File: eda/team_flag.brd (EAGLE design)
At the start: 40.6 x 40.6 mm, 20 parts, among them Q1 MOSFET-LOGIC-NCHANNELSMD, Q2 MOSFET-LOGIC-NCHANNELSMD, U1 ISL83491SOIC, U2 ATTINY1634

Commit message: Add some BOM metadata
* SMA-package diodes
* SOT23-3 MOSFETs
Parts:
- Q1, Q2: value MOSFET-LOGIC-NCHANNELSMD -> IRFML8244; device pie:SOT23-3-LOGIC -> pie:SOT23-3
- R3, R4: value 10K -> 10k
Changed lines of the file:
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@@
 <layer number="1" name="Top" color="4" fill="1" visible="yes" active="yes"/>
 <layer number="2" name="Route2" color="1" fill="3" visible="no" active="no"/>
-<layer number="3" name="Route3" color="4" fill="3" visible="no" active="no"/>
-<layer number="4" name="Route4" color="1" fill="4" visible="no" active="no"/>
+<layer number="3" name="Route3" color="20" fill="3" visible="no" active="no"/>
+<layer number="4" name="Route4" color="21" fill="4" visible="no" active="no"/>
 <layer number="5" name="Route5" color="4" fill="4" visible="no" active="no"/>
 <layer number="6" name="Route6" color="1" fill="8" visible="no" active="no"/>
@@
 <element name="U$2" library="pie" package="OSHW-LOGO-S" value="" x="16.764" y="31.75"/>
 <element name="U$1" library="pie" package="PIE-LOGO-SMALL" value="" x="2.921" y="17.272"/>
-<element name="Q1" library="pie" package="SOT23-3-LOGIC" value="MOSFET-LOGIC-NCHANNELSMD" x="19.304" y="13.208" smashed="yes">
+<element name="Q1" library="pie" package="SOT23-3" value="IRFML8244" x="19.304" y="13.208" smashed="yes">
 <attribute name="NAME" x="22.225" y="14.1097" size="0.635" layer="25" font="vector" rot="R180" align="top-left"/>
-<attribute name="PIE_DIGIKEY-PN" value="DMN65D8L-7DICT-ND" x="19.304" y="13.208" size="1.778" layer="27" display="off"/>
-</element>
-<element name="Q2" library="pie" package="SOT23-3-LOGIC" value="MOSFET-LOGIC-NCHANNELSMD" x="14.224" y="13.208" smashed="yes">
+<attribute name="PIE-INT-REF-NUM" value="NMOS" x="19.304" y="13.208" size="1.778" layer="27" display="off"/>
+</element>
+<element name="Q2" library="pie" package="SOT23-3" value="IRFML8244" x="14.224" y="13.208" smashed="yes">
 <attribute name="NAME" x="17.1704" y="14.1351" size="0.635" layer="25" font="vector" align="bottom-right"/>
-<attribute name="PIE_DIGIKEY-PN" value="DMN65D8L-7DICT-ND" x="14.224" y="13.208" size="1.778" layer="27" display="off"/>
-</element>
-<element name="R3" library="rcl" package="R0603" value="10K" x="24.4094" y="4.064" smashed="yes" rot="R180">
+<attribute name="PIE-INT-REF-NUM" value="NMOS" x="14.224" y="13.208" size="1.778" layer="27" display="off"/>
+</element>
+<element name="R3" library="rcl" package="R0603" value="10k" x="24.4094" y="4.064" smashed="yes" rot="R180">
 <attribute name="NAME" x="24.1046" y="5.7658" size="0.635" layer="25" font="vector" rot="R180"/>
 <attribute name="VALUE" x="25.8826" y="5.7912" size="0.635" layer="27" font="vector" rot="R180"/>
 </element>
-<element name="R4" library="rcl" package="R0603" value="10K" x="28.4734" y="4.064" smashed="yes" rot="R180">
+<element name="R4" library="rcl" package="R0603" value="10k" x="28.4734" y="4.064" smashed="yes" rot="R180">
 <attribute name="NAME" x="27.0002" y="5.1562" size="0.635" layer="25" font="vector" rot="R180" align="top-right"/>
 <attribute name="VALUE" x="28.5242" y="5.1308" size="0.635" layer="27" font="vector" rot="R180" align="top-right"/>

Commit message: Fix having/not having space in part values; add misc resistors
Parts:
- R3, R4: device rcl:R0603 -> pie:R0603
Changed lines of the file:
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@@
 <attribute name="PIE-INT-REF-NUM" value="NMOS" x="14.224" y="13.208" size="1.778" layer="27" display="off"/>
 </element>
-<element name="R3" library="rcl" package="R0603" value="10k" x="24.4094" y="4.064" smashed="yes" rot="R180">
+<element name="R3" library="pie" package="R0603" value="10k" x="24.4094" y="4.064" smashed="yes" rot="R180">
 <attribute name="NAME" x="24.1046" y="5.7658" size="0.635" layer="25" font="vector" rot="R180"/>
 <attribute name="VALUE" x="25.8826" y="5.7912" size="0.635" layer="27" font="vector" rot="R180"/>
+<attribute name="PIE-INT-REF-NUM" value="RESISTOR-GENERIC" x="24.4094" y="4.064" size="1.778" layer="27" rot="R180" display="off"/>
 </element>
-<element name="R4" library="rcl" package="R0603" value="10k" x="28.4734" y="4.064" smashed="yes" rot="R180">
+<element name="R4" library="pie" package="R0603" value="10k" x="28.4734" y="4.064" smashed="yes" rot="R180">
 <attribute name="NAME" x="27.0002" y="5.1562" size="0.635" layer="25" font="vector" rot="R180" align="top-right"/>
 <attribute name="VALUE" x="28.5242" y="5.1308" size="0.635" layer="27" font="vector" rot="R180" align="top-right"/>
+<attribute name="PIE-INT-REF-NUM" value="RESISTOR-GENERIC" x="28.4734" y="4.064" size="1.778" layer="27" rot="R180" display="off"/>
 </element>
 <element name="U1" library="pie" package="SOIC14" value="ISL83491SOIC" x="5.5372" y="7.9502" smashed="yes">

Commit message: Update a bunch more part metadata
Team flag, smartsensor jig, both smartsensors, and controller now have
complete BOM information.
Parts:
- LED1: value (none) -> BLUE
- LED2: value (none) -> YELLOW
- R1, R2: device rcl:R0603 -> pie:R0603
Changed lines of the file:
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@@
 </autorouter>
 <elements>
-<element name="LED1" library="pie" package="LED5MM-NOFLAT" value="" x="20.574" y="20.32" smashed="yes" rot="MR0">
-<attribute name="VALUE" x="17.3736" y="18.5166" size="1.27" layer="28" ratio="10" rot="MR0"/>
+<element name="LED1" library="pie" package="LED5MM-NOFLAT" value="BLUE" x="20.574" y="20.32" smashed="yes" rot="MR0">
+<attribute name="PIE-INT-REF-NUM" value="LED" x="20.574" y="20.32" size="1.778" layer="28" rot="MR0" display="off"/>
 </element>
-<element name="LED2" library="pie" package="LED5MM-NOFLAT" value="" x="12.954" y="20.32" smashed="yes" rot="MR180">
-<attribute name="VALUE" x="16.1544" y="22.1234" size="1.27" layer="28" ratio="10" rot="MR180"/>
+<element name="LED2" library="pie" package="LED5MM-NOFLAT" value="YELLOW" x="12.954" y="20.32" smashed="yes" rot="MR180">
+<attribute name="PIE-INT-REF-NUM" value="LED" x="12.954" y="20.32" size="1.778" layer="28" rot="MR180" display="off"/>
 </element>
-<element name="R1" library="rcl" package="R0603" value="200" x="19.304" y="17.018" smashed="yes" rot="R90">
+<element name="R1" library="pie" package="R0603" value="200" x="19.304" y="17.018" smashed="yes" rot="R90">
 <attribute name="NAME" x="17.526" y="16.7132" size="0.635" layer="25" font="vector" rot="R270"/>
 <attribute name="VALUE" x="18.161" y="18.7452" size="0.635" layer="27" font="vector" rot="R90" align="bottom-right"/>
+<attribute name="PIE-INT-REF-NUM" value="RESISTOR-GENERIC" x="19.304" y="17.018" size="1.778" layer="27" rot="R90" display="off"/>
 </element>
-<element name="R2" library="rcl" package="R0603" value="200" x="14.224" y="17.018" smashed="yes" rot="R90">
+<element name="R2" library="pie" package="R0603" value="200" x="14.224" y="17.018" smashed="yes" rot="R90">
 <attribute name="NAME" x="12.446" y="16.7132" size="0.635" layer="25" font="vector" rot="R270"/>
 <attribute name="VALUE" x="12.4206" y="17.0688" size="0.635" layer="27" font="vector" rot="R270" align="bottom-right"/>
+<attribute name="PIE-INT-REF-NUM" value="RESISTOR-GENERIC" x="14.224" y="17.018" size="1.778" layer="27" rot="R90" display="off"/>
 </element>
 <element name="U$2" library="pie" package="OSHW-LOGO-S" value="" x="16.764" y="31.75"/>

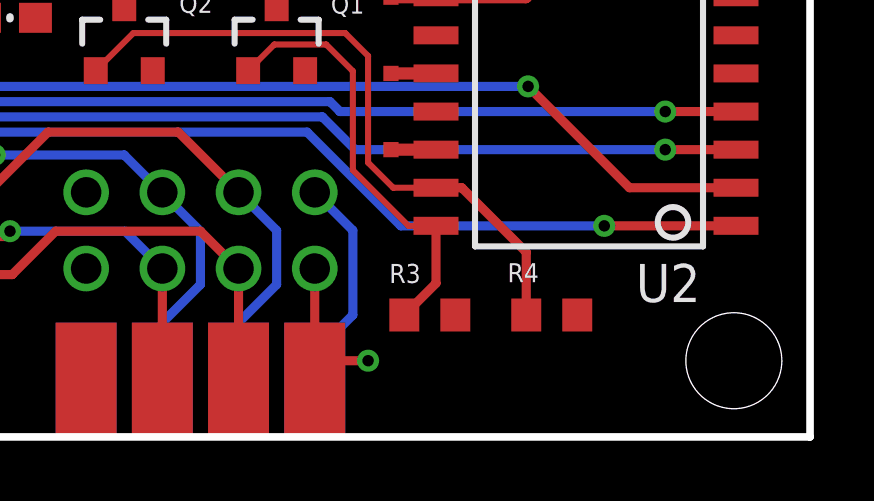
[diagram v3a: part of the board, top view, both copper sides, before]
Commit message: Made battery_buzzer_jig and team_flag_jig.
battery_buzzer_jig incomplete.

Test points added to team flag for the jig
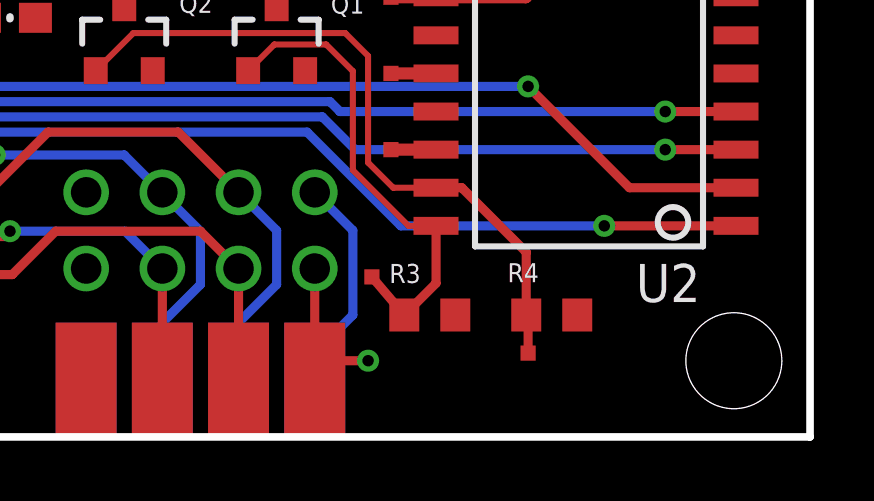
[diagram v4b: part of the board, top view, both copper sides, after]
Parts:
- added TP4, TP5: TEST-POINT2, pie:PAD.02X.02
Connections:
- net BLUE: now also TP5.P$1
- net YELLOW: now also TP4.P$1
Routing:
- net BLUE: track 14.5 -> 16.1 mm
- net YELLOW: track 22.1 -> 23.4 mm
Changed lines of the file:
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@@
 <attribute name="PIE-INT-REF-NUM" value="DNL" x="23.114" y="9.5758" size="1.778" layer="27" display="off"/>
+</element>
+<element name="TP4" library="pie" package="PAD.02X.02" value="TEST-POINT2" x="27.686" y="2.794">
+<attribute name="PIE-INT-REF-NUM" value="DNL" x="27.686" y="2.794" size="1.778" layer="27" display="off"/>
+</element>
+<element name="TP5" library="pie" package="PAD.02X.02" value="TEST-POINT2" x="22.479" y="5.334">
+<attribute name="PIE-INT-REF-NUM" value="DNL" x="22.479" y="5.334" size="1.778" layer="27" display="off"/>
 </element>
 </elements>
@@
 <wire x1="22.352" y1="9.144" x2="23.1902" y2="8.3058" width="0.2032" layer="1"/>
 <wire x1="23.1902" y1="8.3058" x2="24.6164" y2="8.3058" width="0.2032" layer="1"/>
+<contactref element="TP4" pad="P$1"/>
+<wire x1="27.686" y1="2.794" x2="27.686" y2="4.0014" width="0.3048" layer="1"/>
+<wire x1="27.686" y1="4.0014" x2="27.6234" y2="4.064" width="0.3048" layer="1"/>
 </signal>
 <signal name="GND">
@@
 <wire x1="21.844" y1="12.192" x2="20.955" y2="13.081" width="0.2032" layer="1"/>
 <wire x1="19.227" y1="13.081" x2="20.955" y2="13.081" width="0.2032" layer="1"/>
+<contactref element="TP5" pad="P$1"/>
+<wire x1="22.479" y1="5.334" x2="23.5594" y2="4.064" width="0.3048" layer="1"/>
 </signal>
 <signal name="BSOURCE">

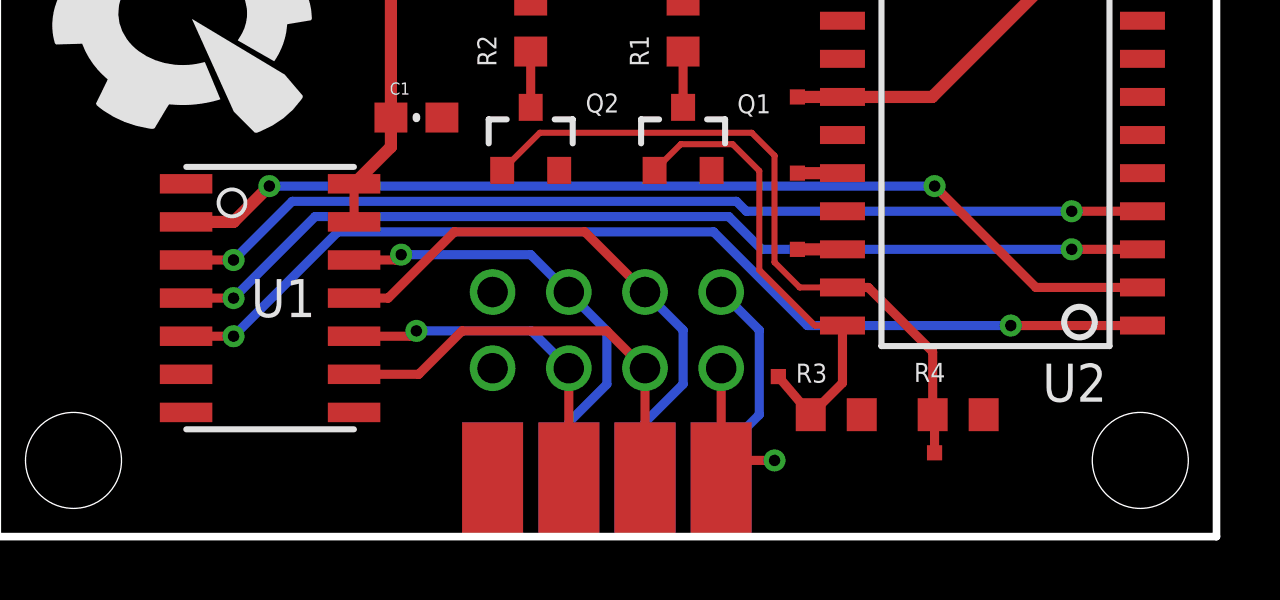
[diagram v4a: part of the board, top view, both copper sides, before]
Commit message: Update all smart-sensor protocol boards to use new pinout
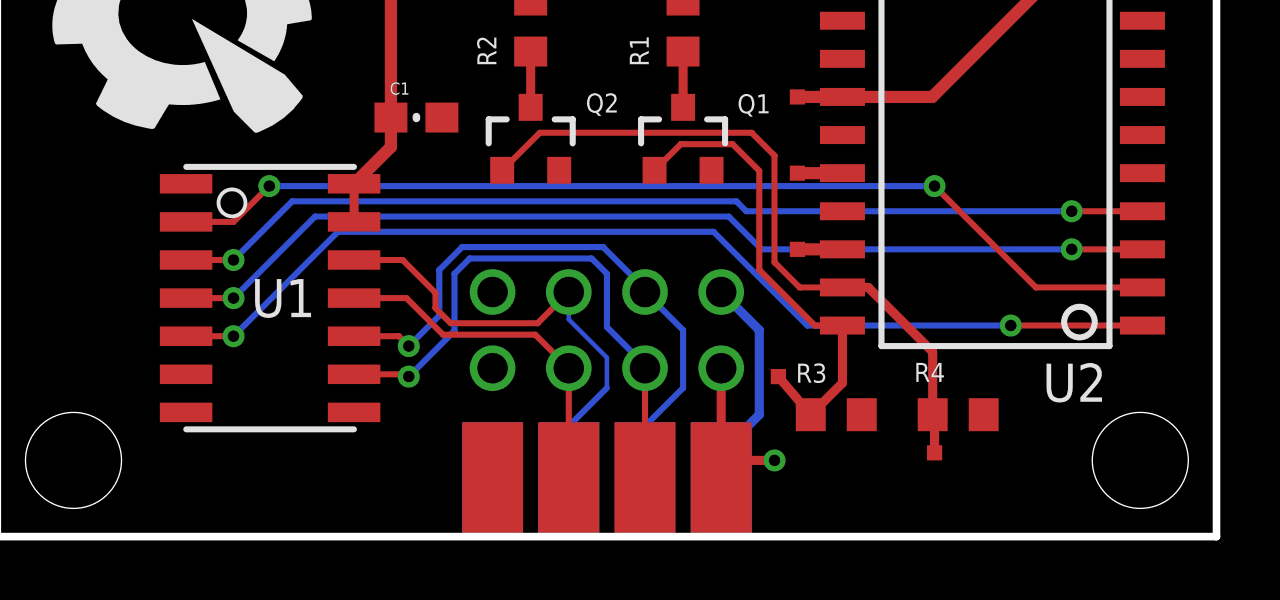
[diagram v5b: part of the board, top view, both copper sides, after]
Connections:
- net A_N: now also U$8.4, U$9.4; no longer U$8.5, U$9.5
- net B_N: now also U$8.5, U$9.5; no longer U$8.4, U$9.4
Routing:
- net B_N: track 11.5 -> 20.1 mm
- net A_N: track 18.7 -> 11.8 mm
- net B_P: track 14.5 -> 18.8 mm, vias 0 -> 1
- net A_P: track 15.0 -> 16.1 mm, vias 1 -> 0

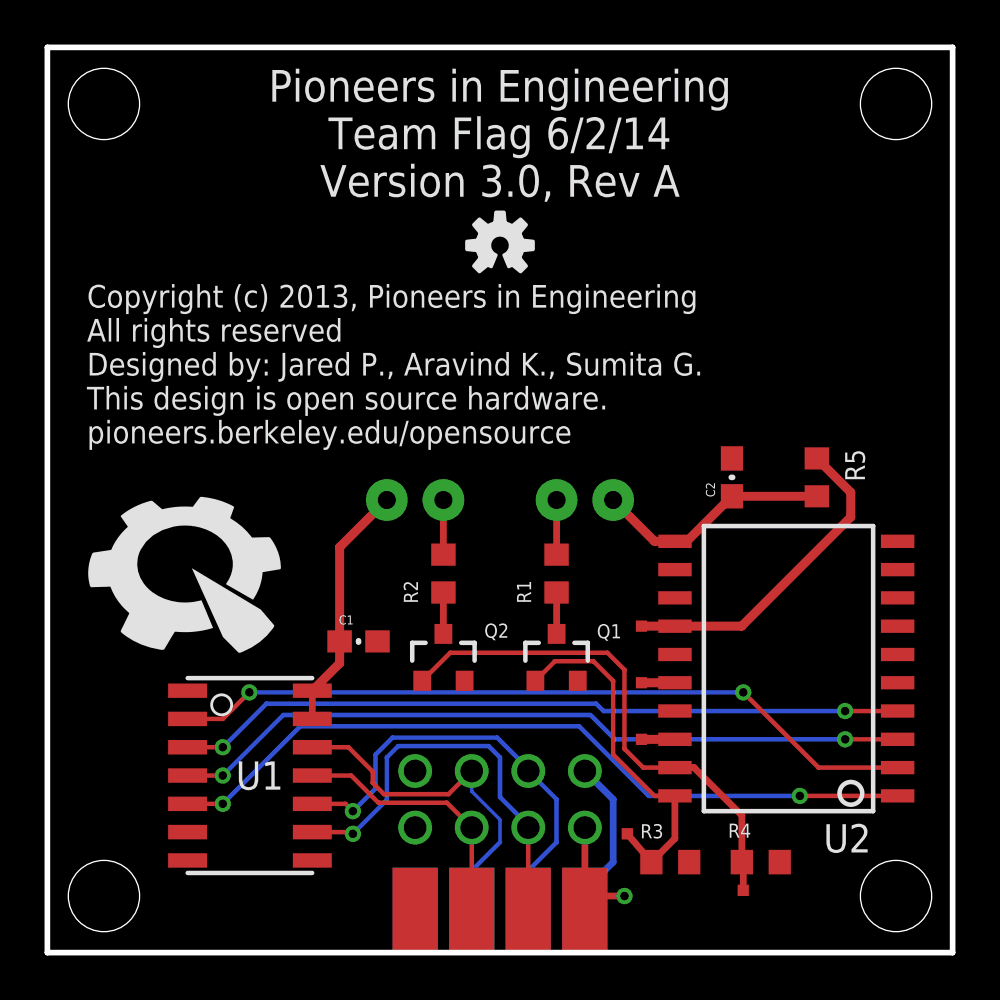
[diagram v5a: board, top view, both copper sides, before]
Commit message: Tiny fixes to team_flag, battery_buzzer, and respective jigs.
To all of them:
- silkscreen font reformatting.
- date in copper layer changed/added.

Board specific:
- team_flag:  test points repositioned.
- team_flag_jig:  test points repositioned; version code added.
- battery_buzzer:  version code added; part values added.
- battery_buzzer_jig:  version code added.
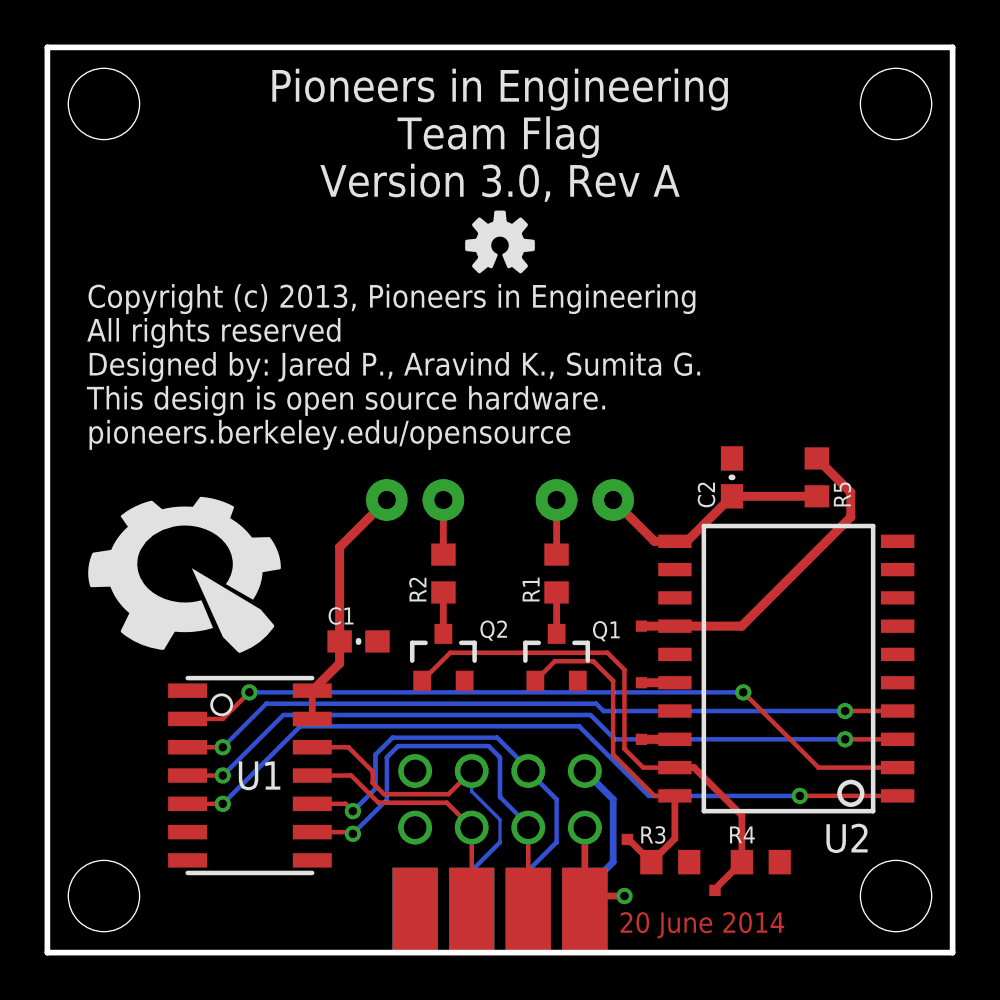
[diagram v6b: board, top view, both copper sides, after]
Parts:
- moved TP4 1.27 mm to (26.4, 2.79)
- moved TP5 0.25 mm to (22.5, 5.08)
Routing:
- net YELLOW: track 23.4 -> 23.9 mm
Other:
- board text added: "20 June 2014"
- board text added: "Pioneers in Engineering Team Flag Version 3.0, Rev A"
- board text removed: "Pioneers in Engineering Team Flag 6/2/14 Version 3.0, Rev A"
